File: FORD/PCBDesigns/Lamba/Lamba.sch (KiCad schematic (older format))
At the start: 15 parts, among them K1 DIP01-1A01-LAMP, K2 DIPx01-1A02-FAN, P1 Digital, P2 COM, P3 ADC, P4 Analog, P5 ADC, Q1 2N2219, Q2 2N2219, U1 NRF24L01_Breakout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

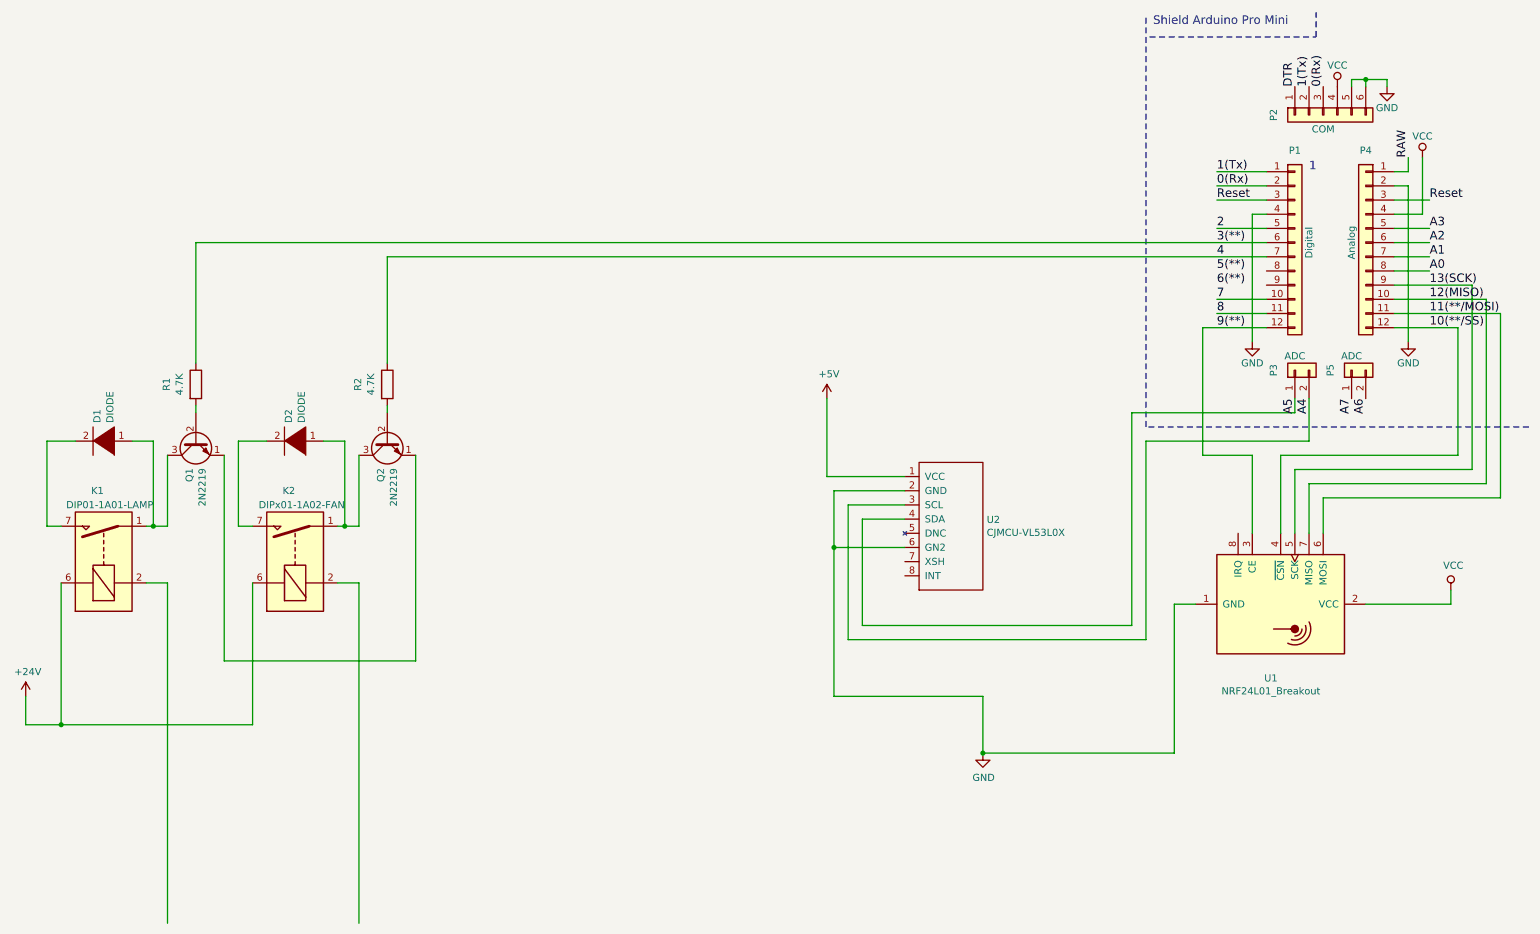
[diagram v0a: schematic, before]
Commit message: Sicaklik mesafe degerleri saçma görünüyor.
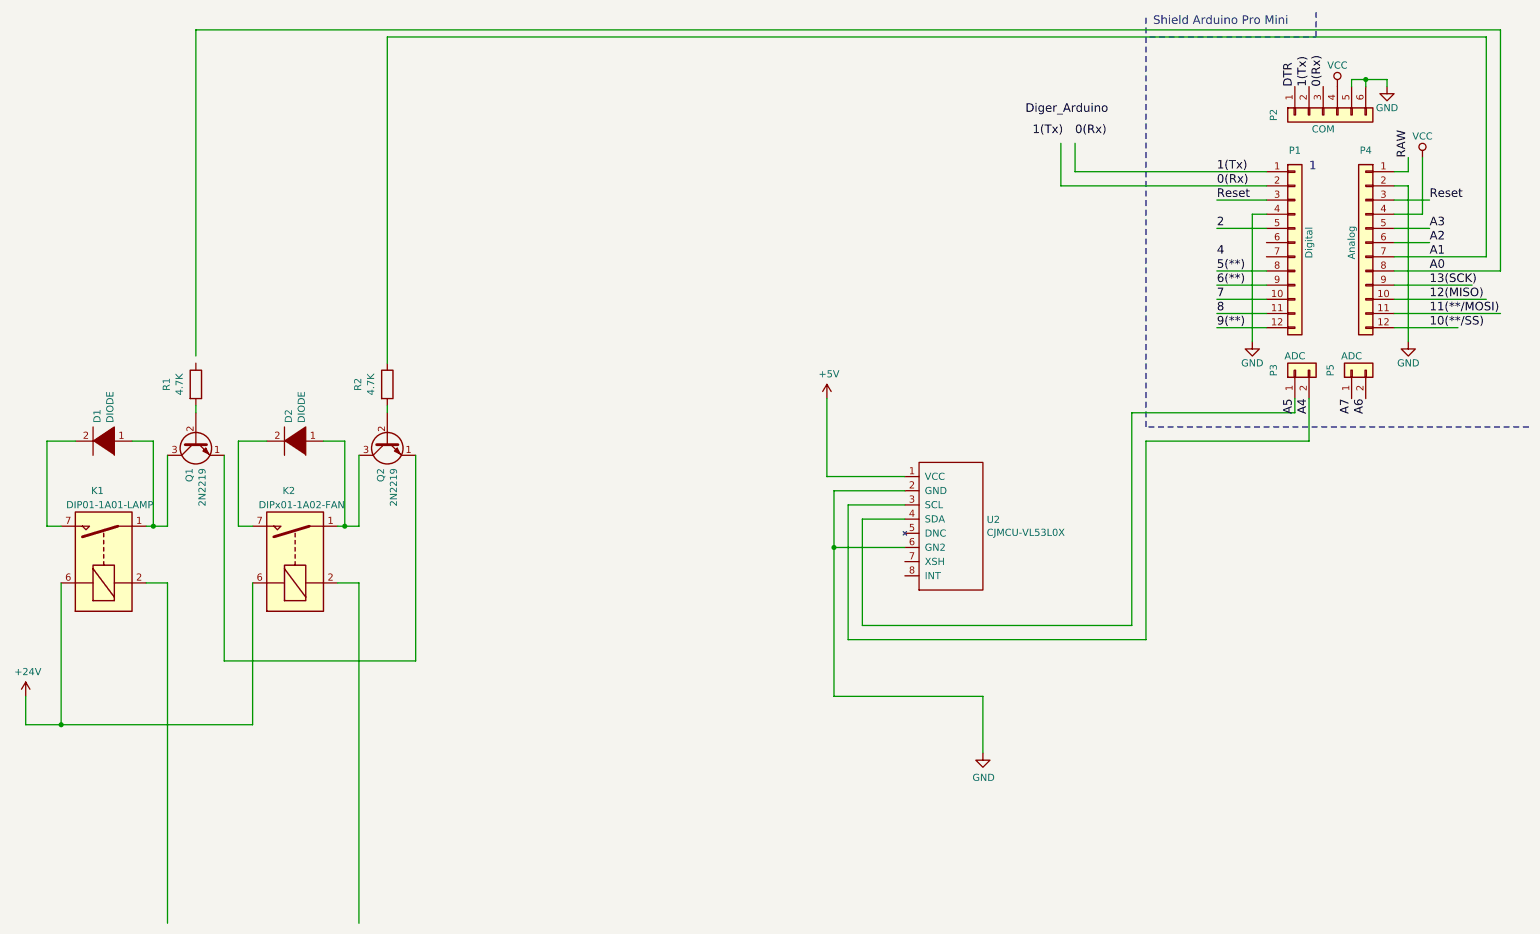
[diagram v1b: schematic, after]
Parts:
- removed U1: NRF24L01_Breakout, RF_Module:nRF24L01_Breakout, symbol RF:NRF24L01_Breakout
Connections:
- net labels added: Diger_Arduino
- net labels removed: 3(**)
- wire segments 103 -> 89
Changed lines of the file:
@@
 Text Label 9000 2000 0    60   ~ 0
 2
-Text Label 9000 2100 0    60   ~ 0
-3(**)
 Text Label 9000 2200 0    60   ~ 0
 4
@@
 	9250 1900 9250 2800
 Wire Wire Line
-	9350 1600 9000 1600
-Wire Wire Line
-	9000 1700 9350 1700
-Wire Wire Line
 	9350 1800 9000 1800
 Wire Wire Line
@@
 Wire Wire Line
 	10250 2100 10500 2100
-Wire Wire Line
-	10500 2200 10250 2200
-Wire Wire Line
-	10250 2300 10500 2300
 Wire Notes Line
 	11200 3400 8500 3400
@@
 	2000 5050 3350 5050
 Wire Wire Line
-	9350 2100 1800 2100
-Wire Wire Line
-	1800 2100 1800 2950
-Wire Wire Line
-	9350 2200 3150 2200
-Wire Wire Line
-	3150 2200 3150 2950
-$Comp
-L RF:NRF24L01_Breakout U1
-U 1 1 5C178728
-P 9450 4650
-F 0 "U1" V 9972 4581 50  0000 C CNN
-F 1 "NRF24L01_Breakout" V 10063 4581 50  0000 C CNN
-F 2 "RF_Module:nRF24L01_Breakout" H 9600 5250 50  0001 L CIN
-F 3 "http://www.nordicsemi.com/eng/content/download/2730/34105/file/nRF24L01_Product_Specification_v2_0.pdf" H 9450 4550 50  0001 C CNN
-	1    9450 4650
-	0    1    1    0
-$EndComp
-Wire Wire Line
-	10650 4650 10050 4650
-Wire Wire Line
-	9750 4150 9750 3900
-Wire Wire Line
-	9750 3900 11000 3900
-Wire Wire Line
-	11000 3900 11000 2600
-Wire Wire Line
 	10250 2600 11000 2600
 Wire Wire Line
-	9650 3800 10900 3800
-Wire Wire Line
-	10900 3800 10900 2500
-Wire Wire Line
 	10250 2500 10900 2500
 Wire Wire Line
-	9650 3800 9650 4150
-Wire Wire Line
-	9550 3700 10800 3700
-Wire Wire Line
-	10800 3700 10800 2400
-Wire Wire Line
 	10250 2400 10800 2400
 Wire Wire Line
-	9550 3700 9550 4150
-Wire Wire Line
-	9450 4150 9450 3600
-Wire Wire Line
-	9450 3600 10700 3600
-Wire Wire Line
-	10700 3600 10700 2700
-Wire Wire Line
 	10250 2700 10700 2700
-Wire Wire Line
-	9250 4150 9250 3600
-Wire Wire Line
-	9250 3600 8900 3600
-Wire Wire Line
-	8900 3600 8900 2700
-Wire Wire Line
-	8900 2700 9350 2700
 $Comp
 L MCU_Module:CJMCU-VL53L0X U2
@@
 $EndComp
 Wire Wire Line
-	8700 4650 8700 5700
-Wire Wire Line
 	6800 3850 6300 3850
 Wire Wire Line
@@
 Wire Wire Line
 	7350 5300 7350 5700
-Connection ~ 7350 5700
 Wire Wire Line
 	6800 4250 6300 4250
@@
 Wire Wire Line
 	6300 4250 6300 5300
-$Comp
-L power:VCC #PWR0104
-U 1 1 5C14ABD4
-P 10650 4550
-F 0 "#PWR0104" H 10650 4400 50  0001 C CNN
-F 1 "VCC" H 10667 4723 50  0000 C CNN
-F 2 "" H 10650 4550 50  0001 C CNN
-F 3 "" H 10650 4550 50  0001 C CNN
-	1    10650 4550
-	1    0    0    -1
-$EndComp
 Wire Wire Line
 	600  5500 600  5300
@@
 Wire Wire Line
 	2950 4500 2800 4500
-Wire Wire Line
-	8700 5700 7350 5700
-Wire Wire Line
-	8850 4650 8700 4650
-Wire Wire Line
-	10650 4650 10650 4550
 $Comp
 L power:+5V #PWR0102
@@
 Wire Wire Line
 	6250 3750 6800 3750
+Wire Wire Line
+	9350 2700 9000 2700
+Wire Wire Line
+	9350 2300 9000 2300
+Wire Wire Line
+	9350 2400 9000 2400
+Wire Wire Line
+	8000 1600 8000 1400
+Wire Wire Line
+	8000 1600 9350 1600
+Wire Wire Line
+	7900 1700 7900 1400
+Wire Wire Line
+	7900 1700 9350 1700
+Text Label 7700 1350 0    60   ~ 0
+1(Tx)
+Text Label 8000 1350 0    60   ~ 0
+0(Rx)
+Text Label 7650 1200 0    60   ~ 0
+Diger_Arduino
+Wire Wire Line
+	1800 2900 1800 600
+Wire Wire Line
+	1800 600  11000 600
+Wire Wire Line
+	11000 600  11000 2300
+Wire Wire Line
+	10250 2300 11000 2300
+Wire Wire Line
+	10900 2200 10900 650
+Wire Wire Line
+	10900 650  3150 650
+Wire Wire Line
+	10250 2200 10900 2200
+Wire Wire Line
+	3150 650  3150 2950
 $EndSCHEMATC
